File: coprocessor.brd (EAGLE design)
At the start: 33 x 53.3 mm, 50 parts, among them IC1 MEGA32U2, U1 TPS61090RSAR, U3 V_REG_LDOSMD2, U4 AZV321

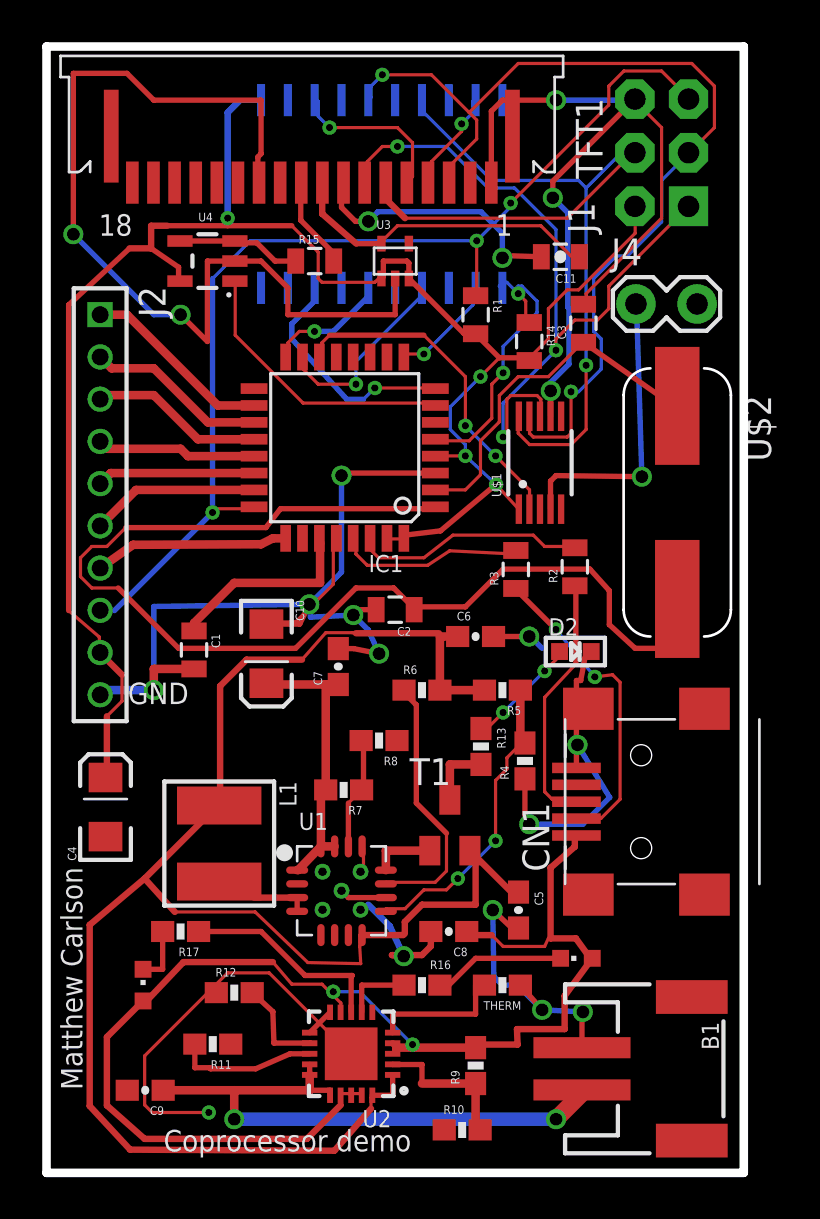
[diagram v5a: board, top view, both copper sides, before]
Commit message: updated the gerbers- fixed the pour and a few clearance issues.
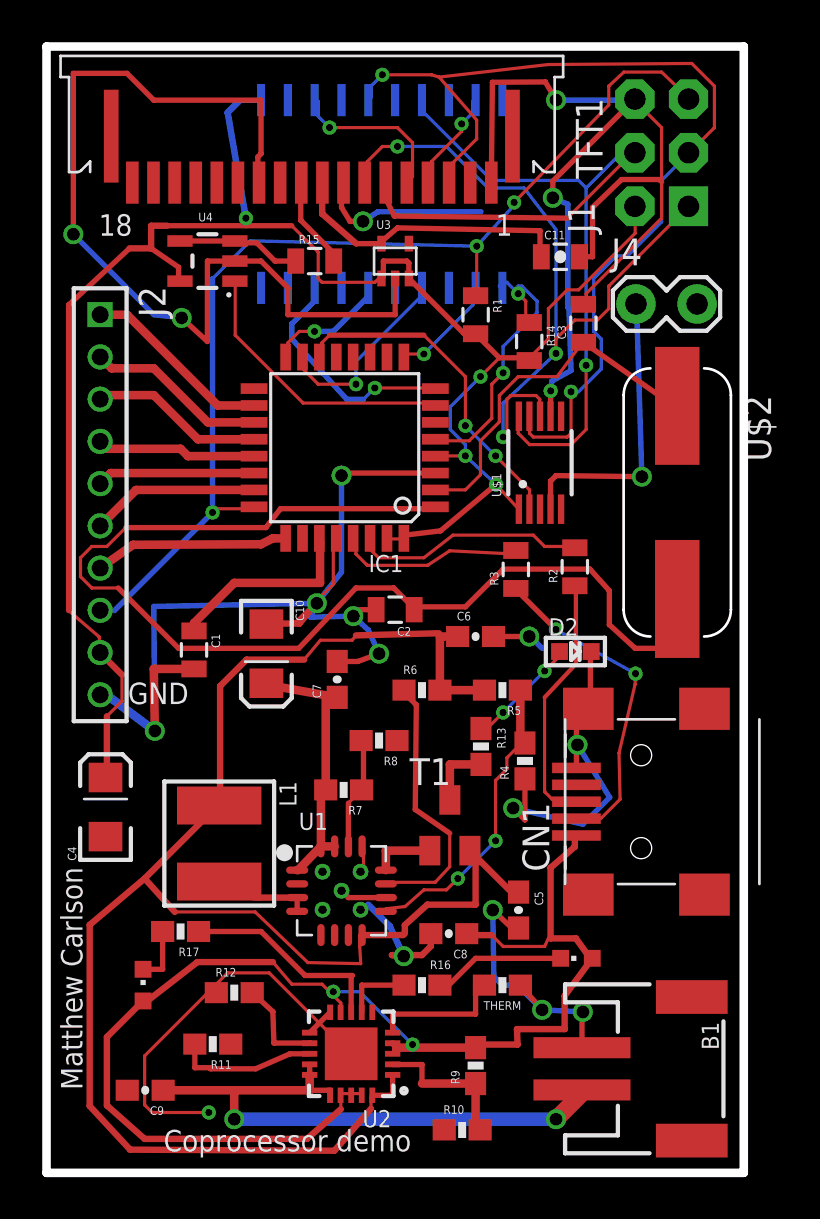
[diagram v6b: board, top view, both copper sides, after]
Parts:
- moved C7 0.61 mm to (13.8, 23.4)
- moved C8 0.10 mm to (19.1, 11.3)
- turned C11 to 0 degrees
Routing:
- net GND: track 203.6 -> 214.6 mm, vias 20 -> 19
- net 2.8V: track 15.2 -> 13.9 mm
- net 5V: track 14.8 -> 14.2 mm
- net DATA-: track 15.0 -> 15.5 mm
- net SCK: track 46.3 -> 46.9 mm

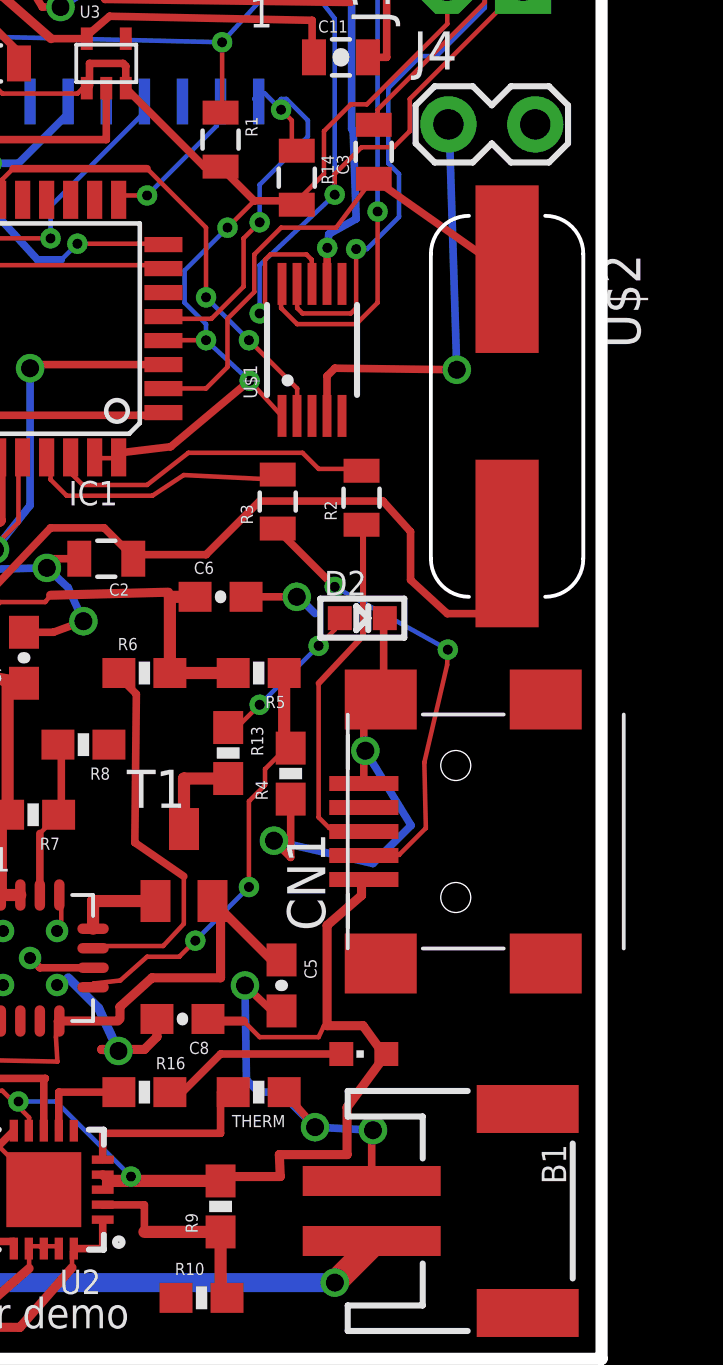
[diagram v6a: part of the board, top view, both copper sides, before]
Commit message: updated the crystal layout
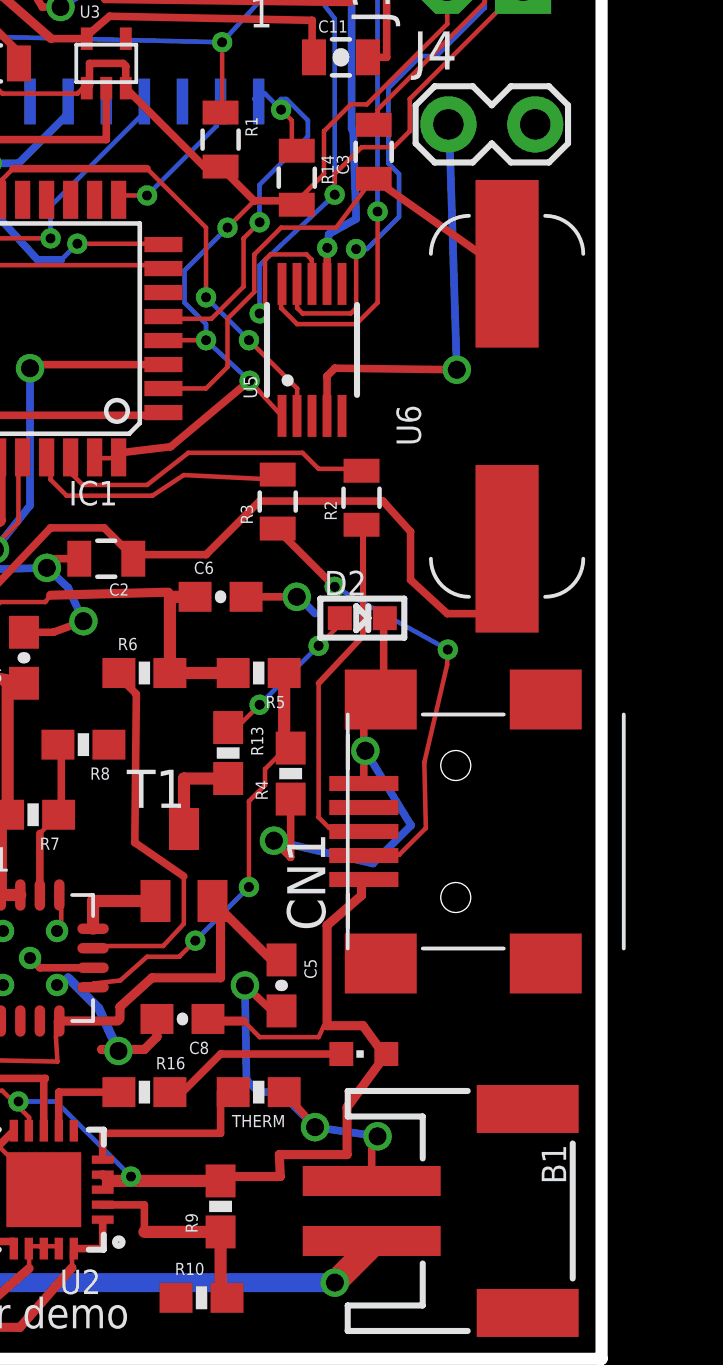
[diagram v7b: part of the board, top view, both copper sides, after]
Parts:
- U5: value MCP48FEB01-E/UN -> MCP48
- renumbered U$1 to U5, U$2 to U6, U$3 to U7
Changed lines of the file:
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@@
 <element name="J2" library="SparkFun-Connectors" package="1X10-2MM" value="" x="2.54" y="40.64" rot="R270"/>
 <element name="C4" library="SparkFun-Capacitors" package="EIA3216" value="10uF" x="2.794" y="17.3228" rot="R90"/>
-<element name="U$1" library="custom" package="10-MSOP" value="MCP48FEB01-E/UN" x="23.368" y="33.6296" rot="R90"/>
+<element name="U5" library="custom" package="10-MSOP" value="MCP48" x="23.368" y="33.6296" rot="R90"/>
 <element name="J4" library="SparkFun-Connectors" package="1X02_LOCK" value="" x="28.0924" y="41.148"/>
-<element name="U$2" library="custom" package="HC49/US" value="16MHZ" x="29.8704" y="31.75" rot="R270"/>
+<element name="U6" library="custom" package="HC49/US" value="16MHZ" x="29.8704" y="31.75" smashed="yes" rot="R270">
+<attribute name="NAME" x="26.1874" y="31.8008" size="0.8128" layer="25" rot="R270"/>
+<attribute name="VALUE" x="26.0604" y="36.83" size="0.8128" layer="27" rot="R270"/>
+</element>
 <element name="R4" library="SparkFun-Resistors" package="0603-RES" value="340k" x="22.6568" y="19.5072" rot="R90">
 <attribute name="PROD_ID" value="RES-12616" x="22.6568" y="19.5072" size="1.778" layer="27" rot="R90" display="off"/>
@@
 <element name="C10" library="SparkFun-Capacitors" package="EIA3216" value="100uF" x="10.414" y="24.5872" rot="R270"/>
 <element name="TFT1" library="custom" package="TFT-CONN-18" value="TFT-18-1.0MM" x="12.065" y="48.895" rot="R180"/>
-<element name="U$3" library="custom" package="S020-75MM" value="CBT3244AD" x="21.59" y="45.72" rot="MR90"/>
+<element name="U7" library="custom" package="S020-75MM" value="CBT3244AD" x="21.59" y="45.72" rot="MR90"/>
 <element name="R14" library="SparkFun-Resistors" package="0805" value="5k" x="22.86" y="39.37" rot="R270"/>
 <element name="U3" library="SparkFun-PowerIC" package="SC70" value="V_REG_LDOSMD2" x="16.51" y="43.18">
@@
 <contactref element="C3" pad="2"/>
 <contactref element="C4" pad="C"/>
-<contactref element="U$1" pad="7"/>
+<contactref element="U5" pad="7"/>
 <contactref element="J4" pad="2"/>
 <polygon width="0.4064" layer="1" isolate="0.3556" orphans="yes">
@@
 <vertex x="0" y="0"/>
 </polygon>
-<contactref element="U$3" pad="P$10"/>
+<contactref element="U7" pad="P$10"/>
 <contactref element="TFT1" pad="1"/>
 <contactref element="TFT1" pad="8"/>
@@
 <wire x1="14.5288" y1="26.3652" x2="12.4968" y2="26.3144" width="0.254" layer="16"/>
 <wire x1="12.4968" y1="26.3144" x2="12.8016" y2="26.9748" width="0.254" layer="16"/>
-<wire x1="25.3576" y1="5.9276" x2="25.3576" y2="7.5776" width="0.254" layer="1"/>
-<wire x1="25.3576" y1="7.5776" x2="25.4" y2="7.62" width="0.254" layer="1"/>
-<via x="25.4" y="7.62" extent="1-16" drill="0.6"/>
-<wire x1="25.4" y1="7.62" x2="23.4696" y2="7.7216" width="0.254" layer="16"/>
+<wire x1="25.3576" y1="5.9276" x2="25.3576" y2="7.2728" width="0.254" layer="1"/>
+<wire x1="25.3576" y1="7.2728" x2="25.5524" y2="7.4168" width="0.254" layer="1"/>
+<via x="25.5524" y="7.4168" extent="1-16" drill="0.6"/>
+<wire x1="25.5524" y1="7.4168" x2="23.4696" y2="7.7216" width="0.254" layer="16"/>
 <via x="23.4696" y="7.7216" extent="1-16" drill="0.6"/>
 <wire x1="23.4696" y1="7.7216" x2="22.44" y2="8.89" width="0.254" layer="1"/>
@@
 <contactref element="R1" pad="2"/>
 <contactref element="C4" pad="A"/>
-<contactref element="U$1" pad="1"/>
-<contactref element="U$3" pad="P$20"/>
+<contactref element="U5" pad="1"/>
+<contactref element="U7" pad="P$20"/>
 <contactref element="R14" pad="2"/>
 <contactref element="U3" pad="1"/>
@@
 <contactref element="IC1" pad="1"/>
 <contactref element="C2" pad="1"/>
-<contactref element="U$2" pad="P$2"/>
+<contactref element="U6" pad="P$2"/>
 <wire x1="19.8357" y1="26.805" x2="17.5126" y2="26.805" width="0.254" layer="1"/>
 <wire x1="21.6227" y1="28.592" x2="19.8357" y2="26.805" width="0.254" layer="1"/>
@@
 <wire x1="29.8429" y1="27.1624" x2="29.8429" y2="25.7328" width="0.1524" layer="1"/>
 <wire x1="17.5126" y1="26.805" x2="17.41" y2="26.67" width="0.1524" layer="1"/>
-<wire x1="29.8429" y1="27.1624" x2="29.8704" y2="27.178" width="0.1524" layer="1"/>
+<wire x1="29.8429" y1="27.1624" x2="29.8704" y2="27.0002" width="0.1524" layer="1"/>
 <wire x1="11.0794" y1="31.4512" x2="18.4061" y2="31.4512" width="0.254" layer="1"/>
 <wire x1="10.3891" y1="30.5577" x2="11.0794" y2="31.4512" width="0.254" layer="1"/>
@@
 <contactref element="IC1" pad="2"/>
 <contactref element="C3" pad="1"/>
-<contactref element="U$2" pad="P$1"/>
-<wire x1="29.8704" y1="36.322" x2="29.707" y2="36.322" width="0.254" layer="1"/>
+<contactref element="U6" pad="P$1"/>
+<wire x1="29.8704" y1="36.4998" x2="29.707" y2="36.322" width="0.254" layer="1"/>
 <wire x1="29.707" y1="36.322" x2="25.4254" y2="39.3336" width="0.254" layer="1"/>
 <wire x1="19.8357" y1="32.3447" x2="18.5848" y2="32.3447" width="0.1524" layer="1"/>
@@
 <signal name="PB0">
 <contactref element="IC1" pad="14"/>
-<contactref element="U$1" pad="2"/>
+<contactref element="U5" pad="2"/>
 <wire x1="13.0451" y1="39.314" x2="13.0451" y2="38.7779" width="0.1524" layer="1"/>
 <wire x1="13.4025" y1="39.6714" x2="13.0451" y2="39.314" width="0.1524" layer="1"/>
@@
 <signal name="SCK">
 <contactref element="J1" pad="3"/>
-<contactref element="U$1" pad="9"/>
-<contactref element="U$3" pad="P$16"/>
+<contactref element="U5" pad="9"/>
+<contactref element="U7" pad="P$16"/>
 <contactref element="TFT1" pad="3"/>
 <wire x1="15.3682" y1="51.4656" x2="15.3682" y2="50.9295" width="0.1524" layer="16"/>
@@
 <signal name="MISO">
 <contactref element="J1" pad="1"/>
-<contactref element="U$1" pad="8"/>
+<contactref element="U5" pad="8"/>
 <contactref element="TFT1" pad="7"/>
 <wire x1="23.3589" y1="36.6335" x2="23.3589" y2="35.9187" width="0.1524" layer="1"/>
@@
 <signal name="MOSI">
 <contactref element="J1" pad="4"/>
-<contactref element="U$1" pad="10"/>
-<contactref element="U$3" pad="P$14"/>
+<contactref element="U5" pad="10"/>
+<contactref element="U7" pad="P$14"/>
 <contactref element="TFT1" pad="6"/>
 <wire x1="22.3375" y1="35.0252" x2="22.3375" y2="35.74" width="0.1524" layer="1"/>
@@
 </signal>
 <signal name="DAC_VOUT">
-<contactref element="U$1" pad="4"/>
+<contactref element="U5" pad="4"/>
 <contactref element="J4" pad="1"/>
 <wire x1="23.868" y1="31.4296" x2="23.868" y2="32.758" width="0.254" layer="1"/>
@@
 </signal>
 <signal name="MCU_CS">
-<contactref element="U$3" pad="P$2"/>
+<contactref element="U7" pad="P$2"/>
 <contactref element="IC1" pad="9"/>
 <wire x1="17.87" y1="38.7779" x2="16.9765" y2="38.7779" width="0.1524" layer="1"/>
@@
 </signal>
 <signal name="MCU_SCK">
-<contactref element="U$3" pad="P$4"/>
+<contactref element="U7" pad="P$4"/>
 <contactref element="IC1" pad="15"/>
 <wire x1="12.1516" y1="38.0631" x2="12.1516" y2="38.5992" width="0.1524" layer="1"/>
@@
 </signal>
 <signal name="MCU_MOSI">
-<contactref element="U$3" pad="P$6"/>
+<contactref element="U7" pad="P$6"/>
 <contactref element="IC1" pad="16"/>
 <wire x1="11.4368" y1="39.314" x2="11.4368" y2="38.7779" width="0.1524" layer="1"/>
@@
 </signal>
 <signal name="MCU_RS">
-<contactref element="U$3" pad="P$8"/>
+<contactref element="U7" pad="P$8"/>
 <contactref element="IC1" pad="8"/>
 <wire x1="15.5469" y1="37.1696" x2="18.4061" y2="37.1696" width="0.1524" layer="1"/>
@@
 </signal>
 <signal name="PC2">
-<contactref element="U$3" pad="P$1"/>
+<contactref element="U7" pad="P$1"/>
 <contactref element="R14" pad="1"/>
 <contactref element="IC1" pad="5"/>
@@
 <signal name="TFT_RS">
 <contactref element="TFT1" pad="4"/>
-<contactref element="U$3" pad="P$12"/>
+<contactref element="U7" pad="P$12"/>
 <wire x1="20.1931" y1="50.2147" x2="20.1931" y2="50.7508" width="0.1524" layer="16"/>
 <wire x1="19.657" y1="49.6786" x2="20.1931" y2="50.2147" width="0.1524" layer="16"/>
@@
 <signal name="TFT_CS">
 <contactref element="TFT1" pad="5"/>
-<contactref element="U$3" pad="P$18"/>
+<contactref element="U7" pad="P$18"/>
 <wire x1="12.8664" y1="50.036" x2="12.8664" y2="50.7508" width="0.1524" layer="16"/>
 <wire x1="13.4025" y1="49.4999" x2="12.8664" y2="50.036" width="0.1524" layer="16"/>

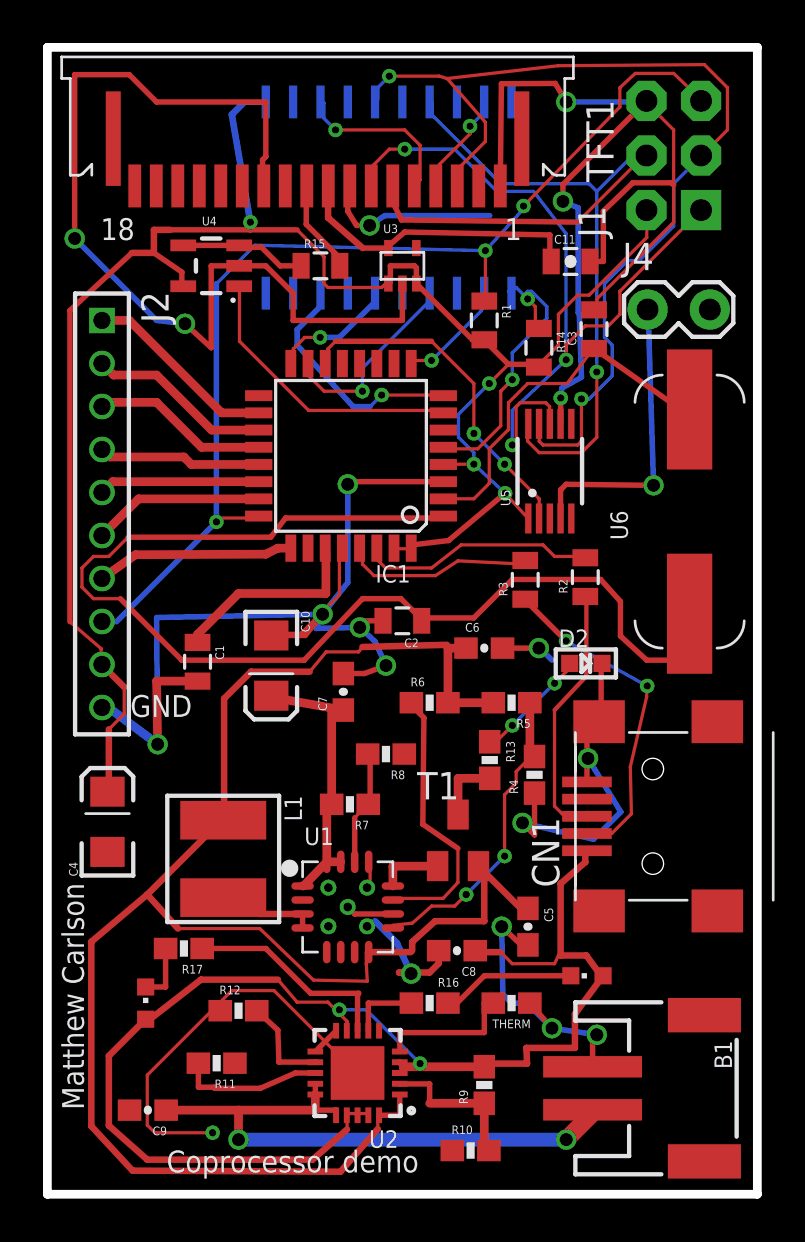
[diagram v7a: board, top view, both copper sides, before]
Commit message: updates to the bus switch package and trace widths
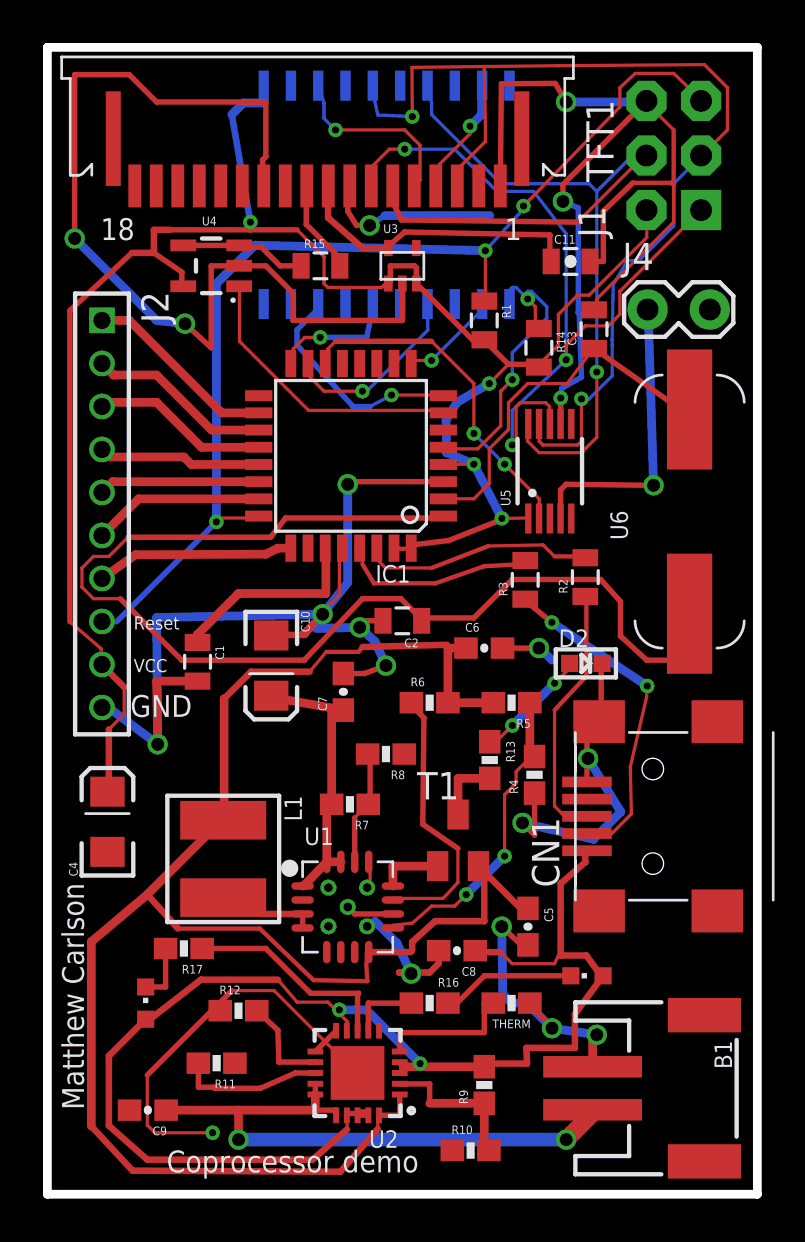
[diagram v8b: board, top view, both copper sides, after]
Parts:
- moved U7 0.77 mm to (21.5, 46.5)
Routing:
- net SCK: track 46.9 -> 49.1 mm
- net VCC: track 89.4 -> 90.7 mm
- net MCU_MOSI: track 5.83 -> 6.77 mm
- net MOSI: track 43.1 -> 43.8 mm
- net TFT_CS: track 7.87 -> 8.55 mm
- net MCU_SCK: track 9.23 -> 9.91 mm
- net TFT_RS: track 4.90 -> 5.57 mm
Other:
- board text added: "Reset"
- board text added: "VCC"
